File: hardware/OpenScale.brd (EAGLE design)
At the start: 54.6 x 40.6 mm, 64 parts, among them Q1 200mA/50V, Q2 200mA/50V, Q3 MMBT4403, U1 HX711, U3 TMP102, U4 ATMEGA328P_TQFP, U6 FT231X, Y2 16MHZ

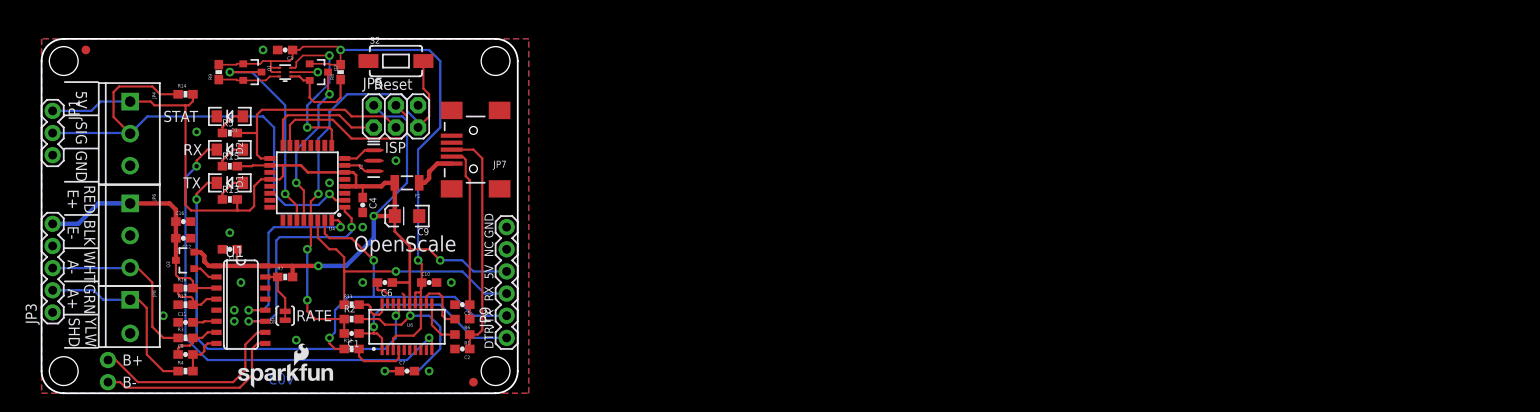
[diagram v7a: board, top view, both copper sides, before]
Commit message: New version with screw terminals. Ready for review.
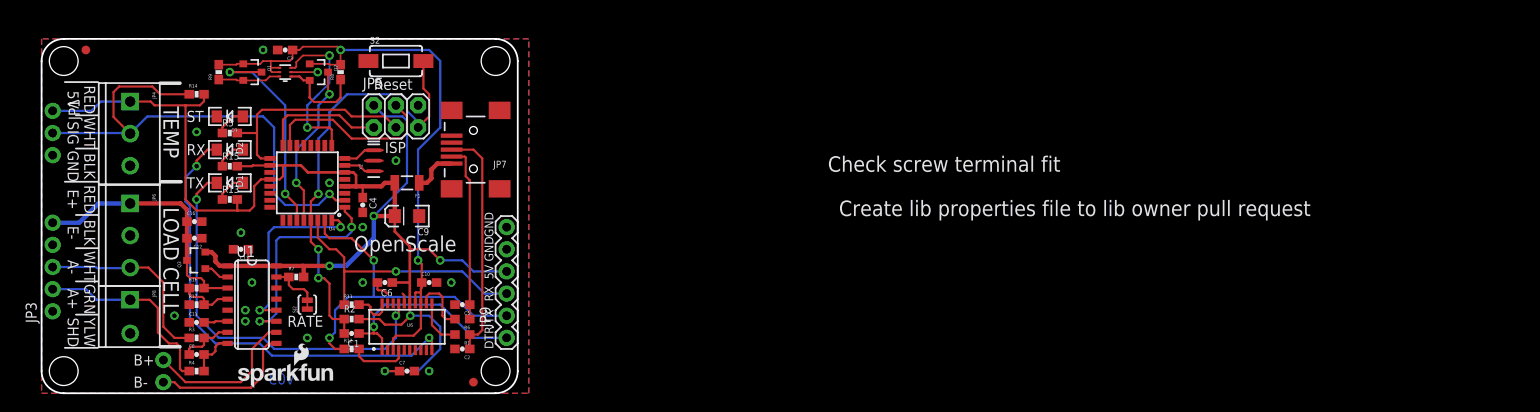
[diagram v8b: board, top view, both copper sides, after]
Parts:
- JP1: device SparkFun-Connectors:1X03 -> SparkFun-Connectors:1X03_NO_SILK
- JP3: device SparkFun-Connectors:1X05 -> SparkFun-Connectors:1X05_NO_SILK
- moved JP2 6.35 mm to (14.0, 3.81)
- moved SJ2 2.84 mm to (30.5, 10.2)
- moved C11 1.27 mm to (17.8, 8.13)
- moved C12 1.27 mm to (17.5, 17.8)
- moved C13 1.27 mm to (22.9, 16.5)
- moved C16 1.27 mm to (17.5, 19.7)
- moved C8 1.27 mm to (17.8, 4.45)
- moved Q3 1.27 mm to (17.8, 15.2)
- moved R14 1.27 mm to (17.8, 34.3)
- moved R16 1.27 mm to (17.8, 12.1)
- moved R17 1.27 mm to (17.8, 10.2)
- moved R3 1.27 mm to (17.8, 6.35)
- moved R4 1.27 mm to (17.8, 2.54)
- moved R7 1.27 mm to (29.2, 13.3)
- moved U1 1.27 mm to (24.1, 10.2)
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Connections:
- net GND: now also JP9.CTS
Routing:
- net B+: track 23.2 -> 17.9 mm
- net B-: track 22.2 -> 17.1 mm
- net TXLED: track 55.3 -> 53.2 mm
- net RXLED: track 47.3 -> 45.9 mm
- net A-: track 20.8 -> 22.1 mm
- net A+: track 21.4 -> 22.7 mm
- net TEMP_DAT: track 57.4 -> 58.7 mm
- net LC_SCK: track 26.0 -> 24.7 mm
- net LC_DOUT: track 22.9 -> 21.6 mm
- net AVDD: track 28.6 -> 29.9 mm
- net RST: track 52.3 -> 51.1 mm
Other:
- board text added: "BLK GND"
- board text added: "Check screw terminal fit"
- board text added: "Create lib properties file to lib owner pull request"
- board text added: "LOAD CELL"
- board text added: "RED 5V"
- board text added: "ST"
- board text added: "TEMP"
- board text added: "WHT SIG"
- board text removed: "NC"
- board text removed: "STAT"
